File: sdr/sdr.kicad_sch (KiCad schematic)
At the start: 2 parts, among them J3 Conn_Coaxial, U5 BGA2817

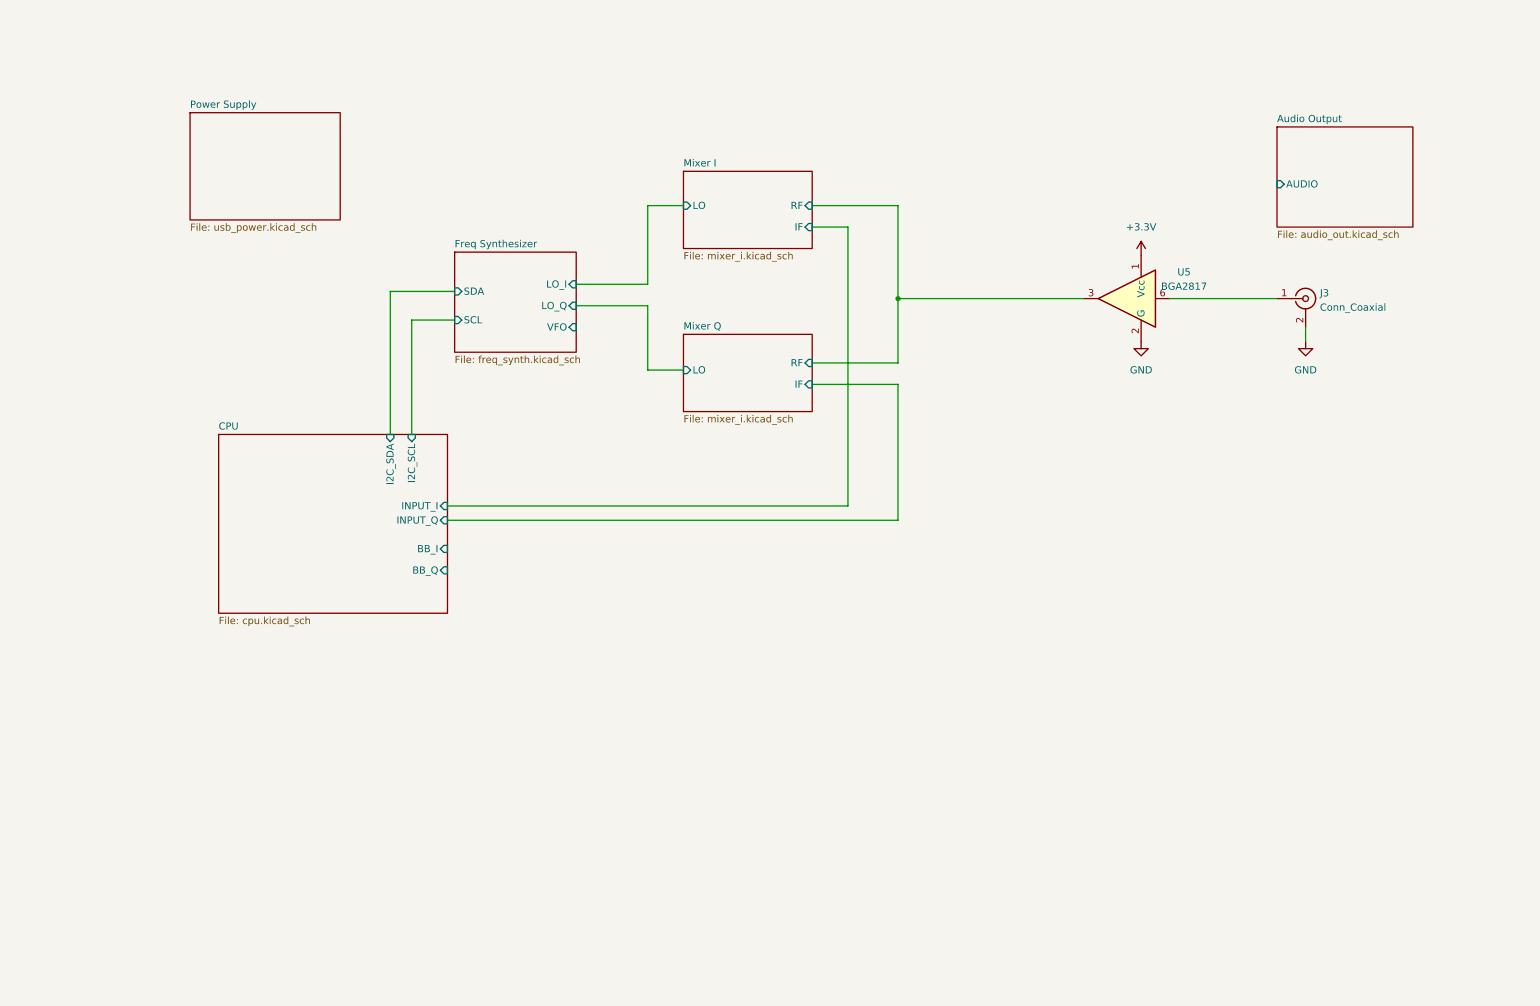
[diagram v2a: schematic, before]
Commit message: Added ST-link 6-pin 0.1 programming header
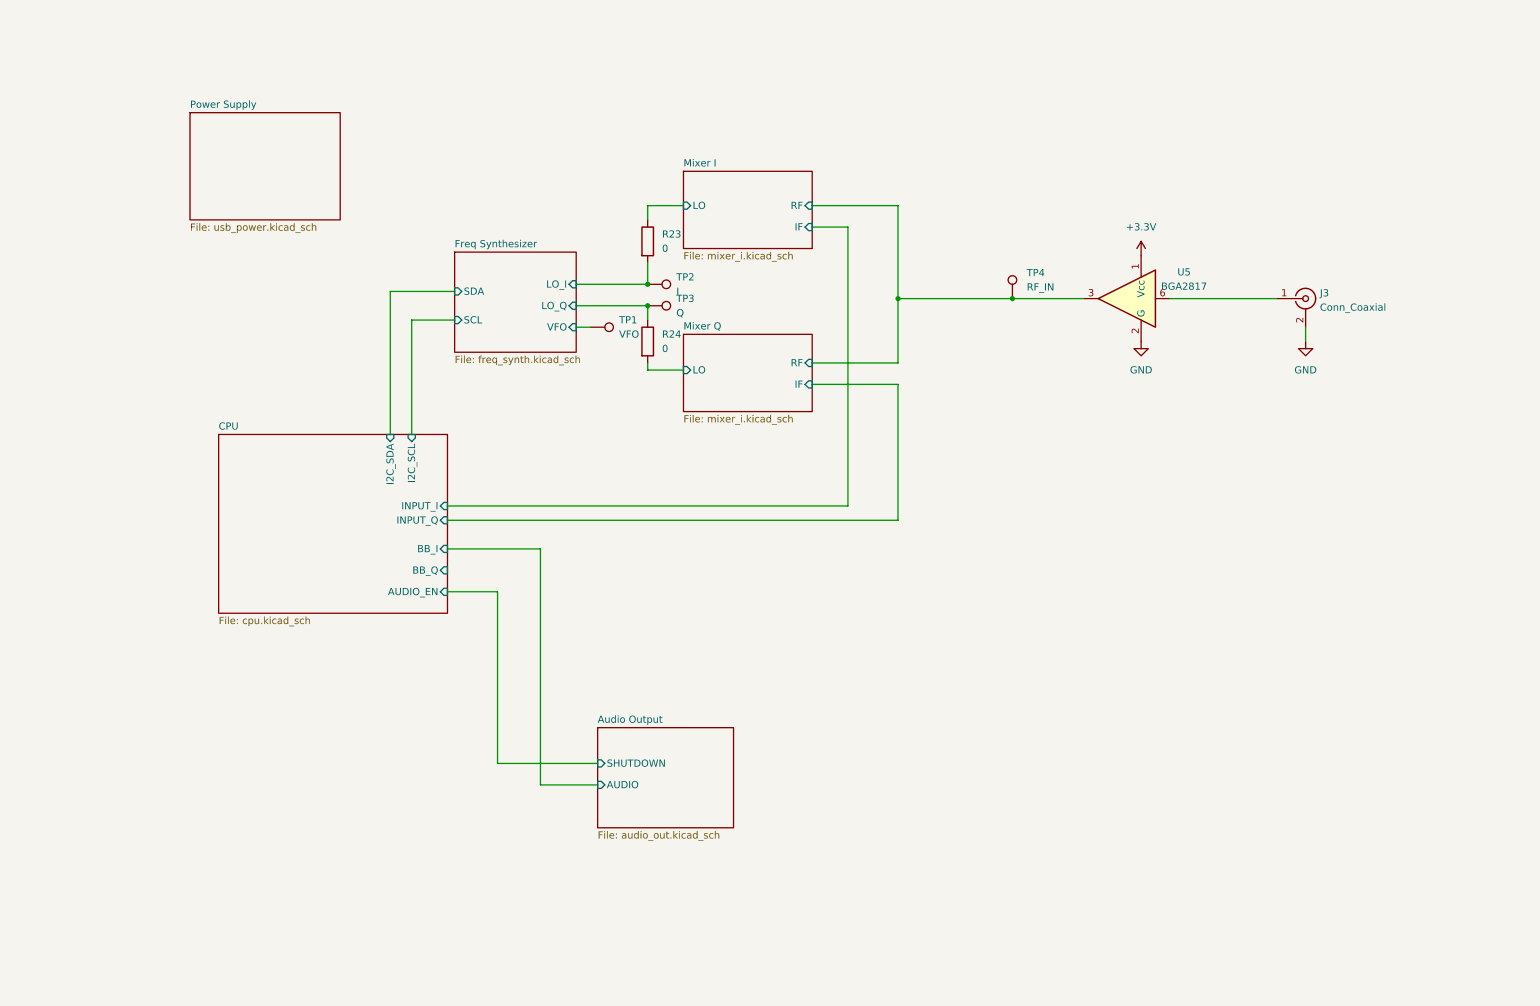
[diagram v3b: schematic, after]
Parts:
- added R23, R24: 0, Resistor_SMD:R_0402_1005Metric, symbol Device:R
- added TP1: VFO, TestPoint:TestPoint_Pad_D1.0mm, symbol Connector:TestPoint
- added TP2: I, TestPoint:TestPoint_Pad_D1.0mm, symbol Connector:TestPoint
- added TP3: Q, TestPoint:TestPoint_Pad_D1.0mm, symbol Connector:TestPoint
- added TP4: RF_IN, TestPoint:TestPoint_Pad_D1.0mm, symbol Connector:TestPoint
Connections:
- net Freq Synthesizer/LO_I: now also R23.2, TP2.1
- net Freq Synthesizer/LO_Q: now also R24.1, TP3.1
- net Freq Synthesizer/VFO: now also TP1.1
- net Mixer I/RF: now also TP4.1
- new net Mixer I/LO: R23.1
- new net Mixer Q/LO: R24.2
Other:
- sheet Audio Output ports: added SHUTDOWN; removed none
- sheet CPU ports: added AUDIO_EN; removed none

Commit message: Tighten up design layout.
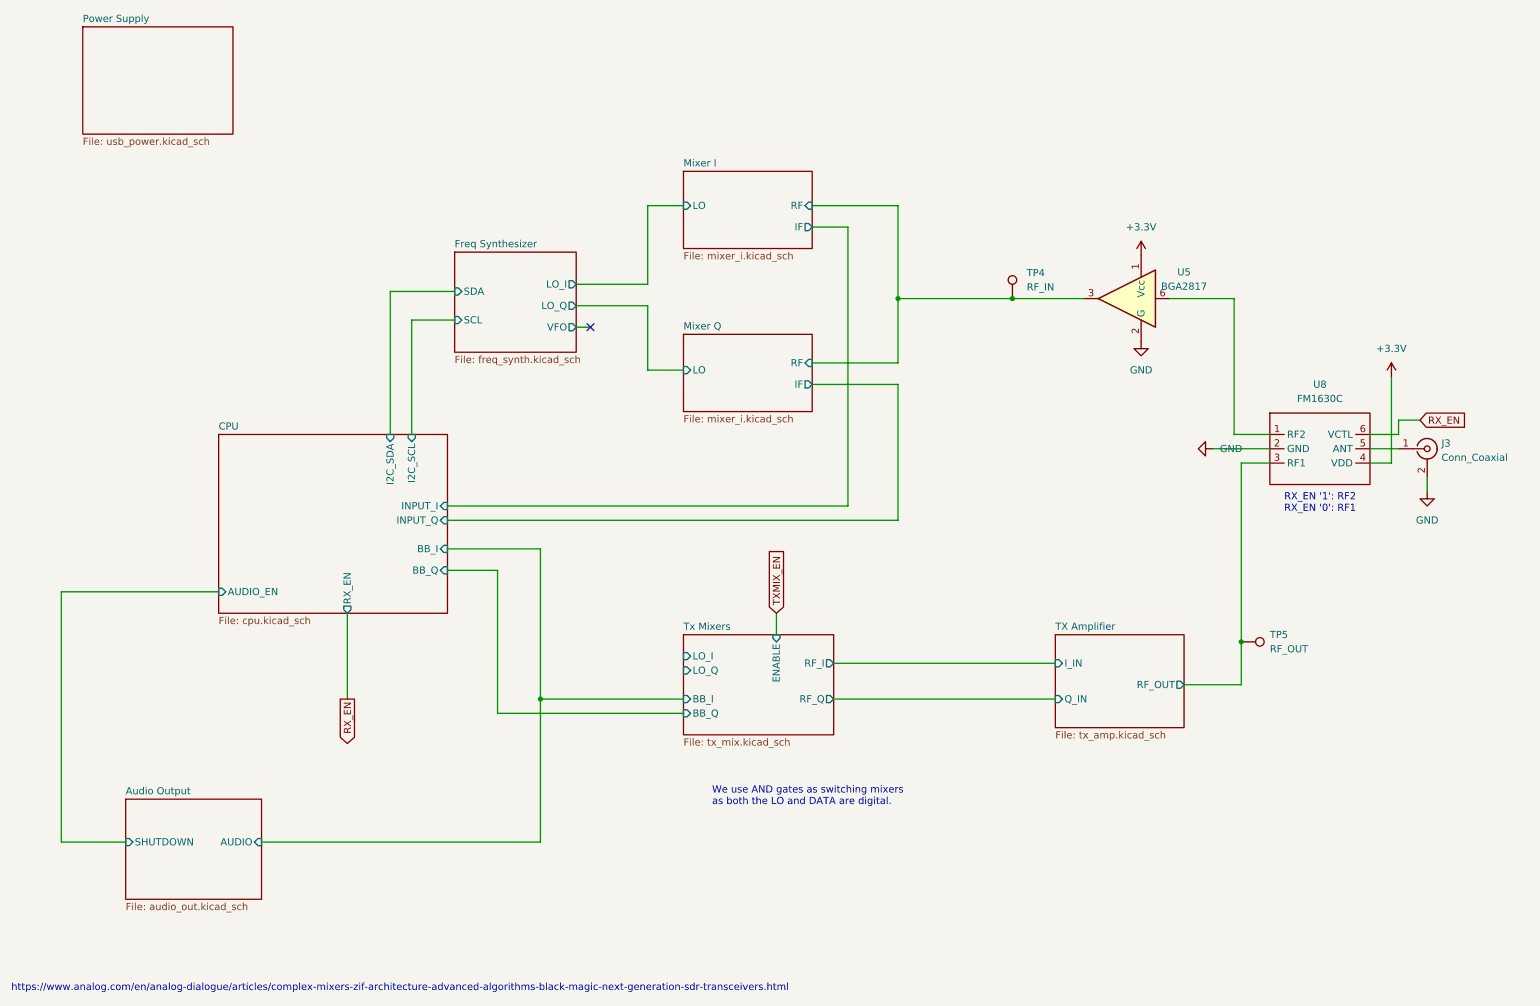
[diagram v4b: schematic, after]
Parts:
- removed R23, R24: 0, Resistor_SMD:R_0402_1005Metric, symbol Device:R
- removed TP1: VFO, TestPoint:TestPoint_Pad_D1.0mm, symbol Connector:TestPoint
- removed TP2: I, TestPoint:TestPoint_Pad_D1.0mm, symbol Connector:TestPoint
- removed TP3: Q, TestPoint:TestPoint_Pad_D1.0mm, symbol Connector:TestPoint
- added TP5: RF_OUT, TestPoint:TestPoint_Pad_D1.0mm, symbol Connector:TestPoint
- added U8: FM1630C, ZL4AA:DFN-6_L1.1-W0.7-P0.40-BL, symbol zl4aa:FM1630C
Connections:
- net +3.3V: now also U8.4 (VDD)
- net GND: now also U8.2 (GND)
- net at J3.1 (In): now also U8.5 (ANT); no longer U5.6
- new net: U5.6, U8.1 (RF2)
- new net RX_EN: U8.6 (VCTL)
- new net TX Amplifier/RF_OUT: TP5.1, U8.3 (RF1)
- no-connect marks 0 -> 1
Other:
- added sheet TX Amplifier (tx_amp.kicad_sch)
- added sheet Tx Mixers (tx_mix.kicad_sch)
- sheet CPU ports: added RX_EN; removed none
- note added: "RX_EN '1': RF2 RX_EN '0': RF1"
- note added: "We use AND gates as switching mixers as both the LO and DATA are digital."
- note added: "https://www.analog.com/en/analog-dialogue/articles/complex-mixers-zif-architecture-advanced-algorithms-black-magic-next-generation-sdr-transceivers.html"
- moved on the sheet: J3

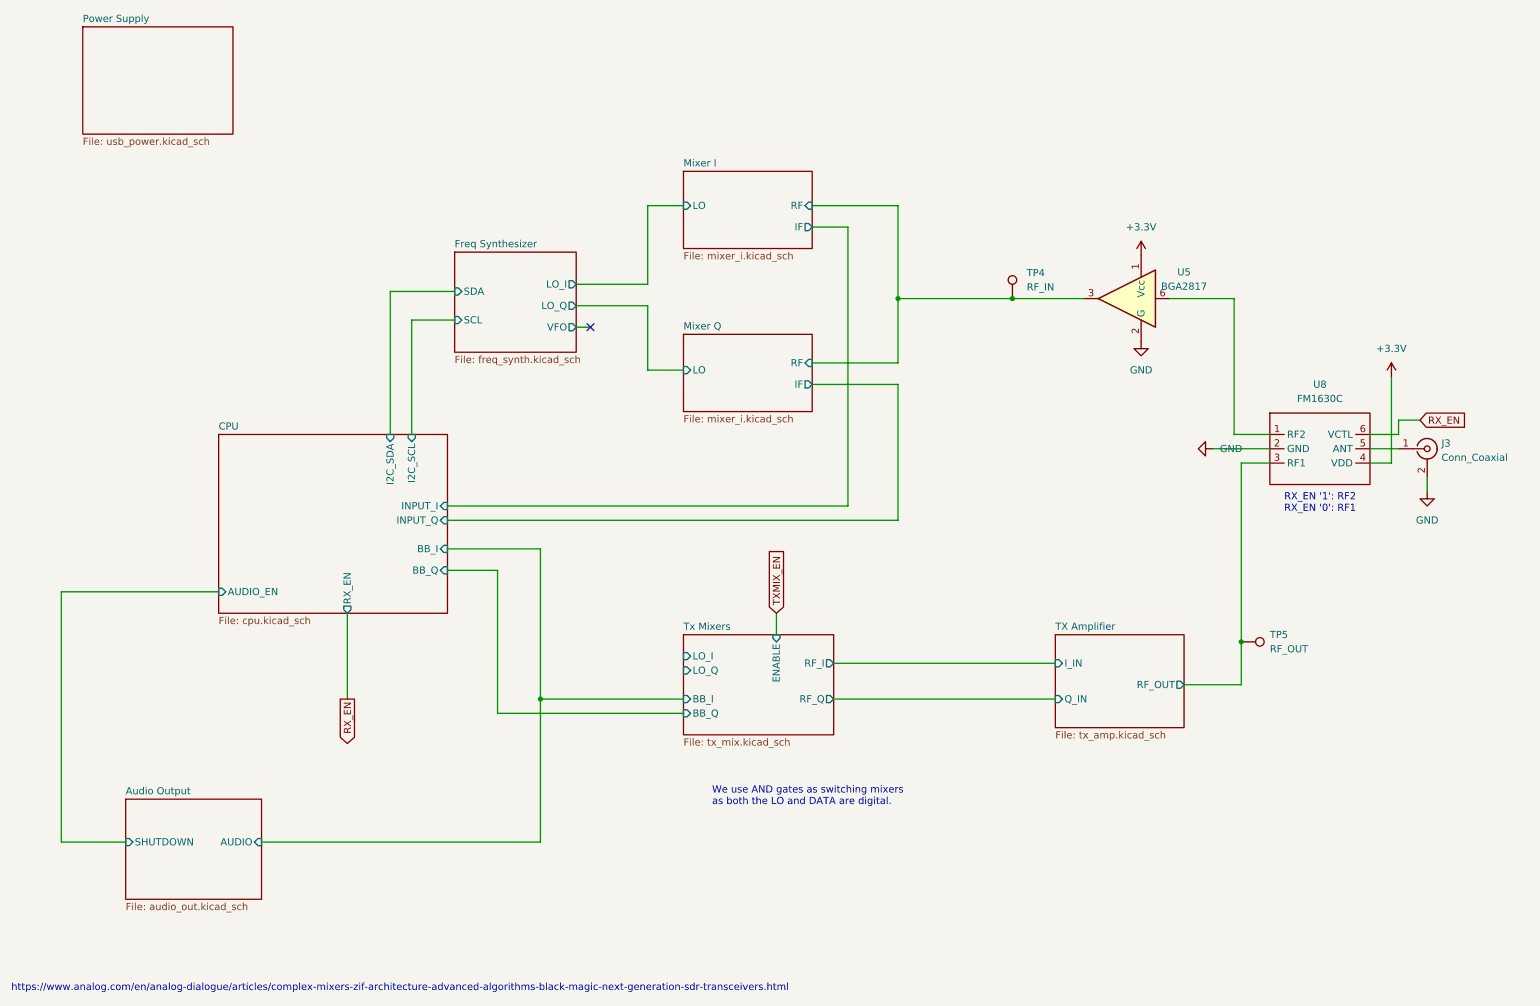
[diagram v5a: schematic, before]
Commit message: Many fixes. Updated mixers to use the analog switches rather than discretes.
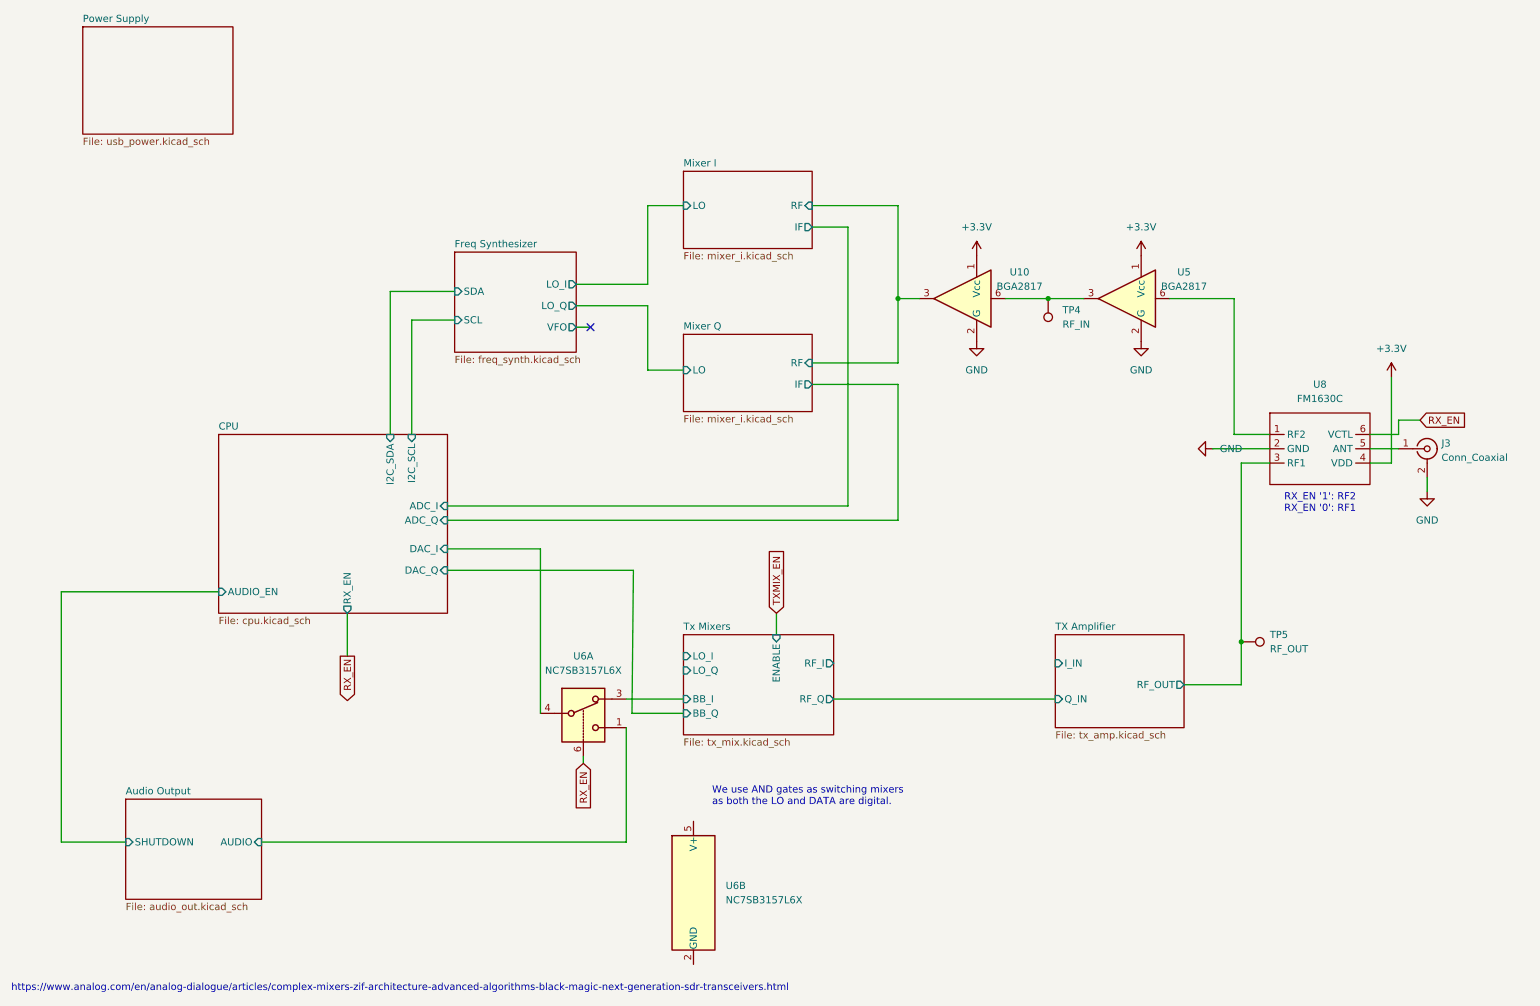
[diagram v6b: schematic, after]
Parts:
- added U10: BGA2817, Package_TO_SOT_SMD:SOT-363_SC-70-6, symbol RF_Amplifier:BGA2817
- added U6: NC7SB3157L6X, Package_SON:Fairchild_MicroPak-6_1.0x1.45mm_P0.5mm, symbol Analog_Switch:NC7SB3157L6X
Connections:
- net +3.3V: now also U10.1 (Vcc)
- net Audio Output/AUDIO: now also U6.1
- net GND: now also U10.2 (G), U10.4 (G), U10.5 (G)
- net Mixer I/RF: now also U10.3; no longer TP4.1, U5.3
- net RX_EN: now also U6.6
- new net: TP4.1, U10.6, U5.3
- new net CPU/DAC_I: U6.4
- new net Tx Mixers/BB_I: U6.3
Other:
- sheet CPU ports: added ADC_I, ADC_Q, DAC_I, DAC_Q; removed BB_I, BB_Q, INPUT_I, INPUT_Q
- moved on the sheet: TP4
